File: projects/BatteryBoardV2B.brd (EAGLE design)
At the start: 90.6 x 96 mm, 225 parts, among them M1 BSO201SP, SW1 BTS50015-1TAD, SW2 BTS50015-1TAD, T1 AD590FLATPACK, T2 AD590FLATPACK, T3 AD590FLATPACK, T4 AD590FLATPACK, U1 TCA9535PWR, U10 LT1962-3, U11 LT1962-3, U12 LTC4411, U13 LTC4411, U14 LTC4121, U15 VNS3NV04DP-E, U16 LTC4121, U17 VNS3NV04DP-E, U18 AD8418, U19 AD8418, U2 AD7991-0, U3 LTC4412MPS6, U4 LTC4121-4.2, U5 LTC4121-4.2, U6 LC05111C13MTTTG, U7 LC05111C13MTTTG, U8 AD8418, U9 AD8418

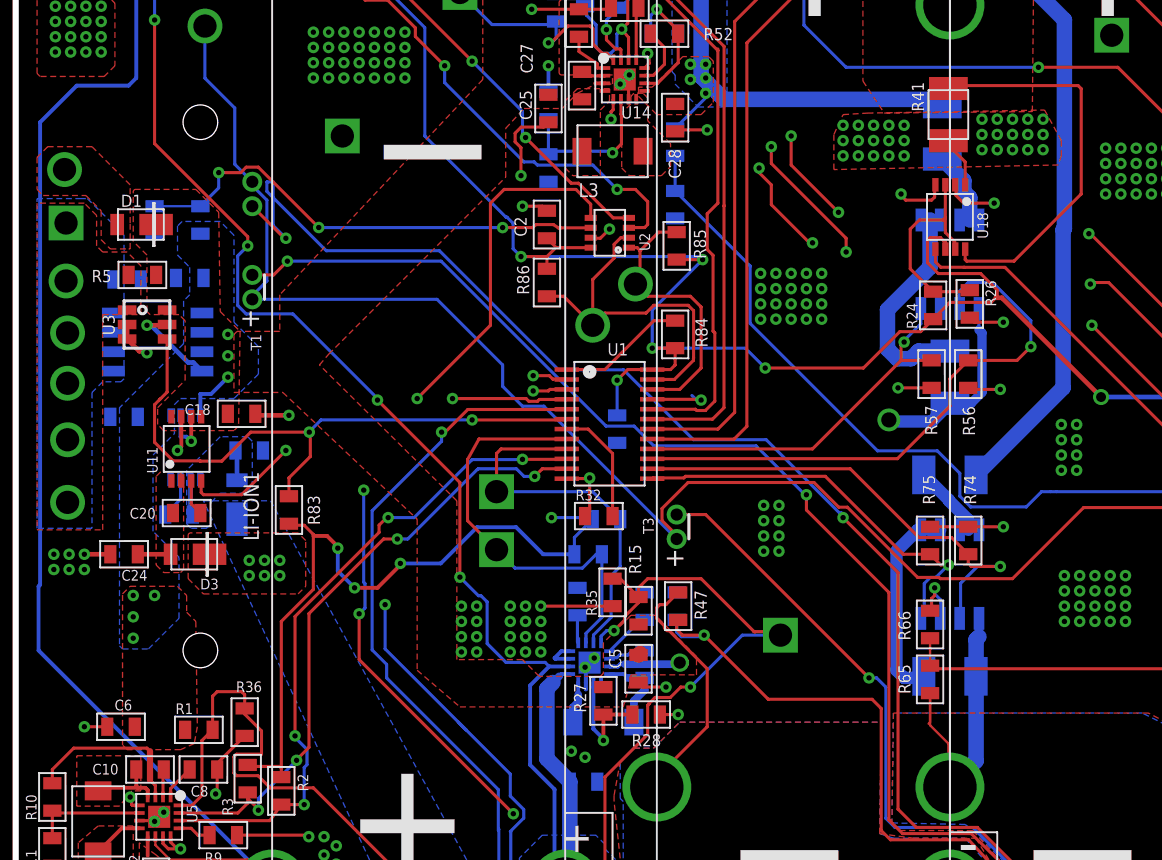
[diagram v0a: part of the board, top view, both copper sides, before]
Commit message: Updating schematic for battery board, adding schematic for flight configuration
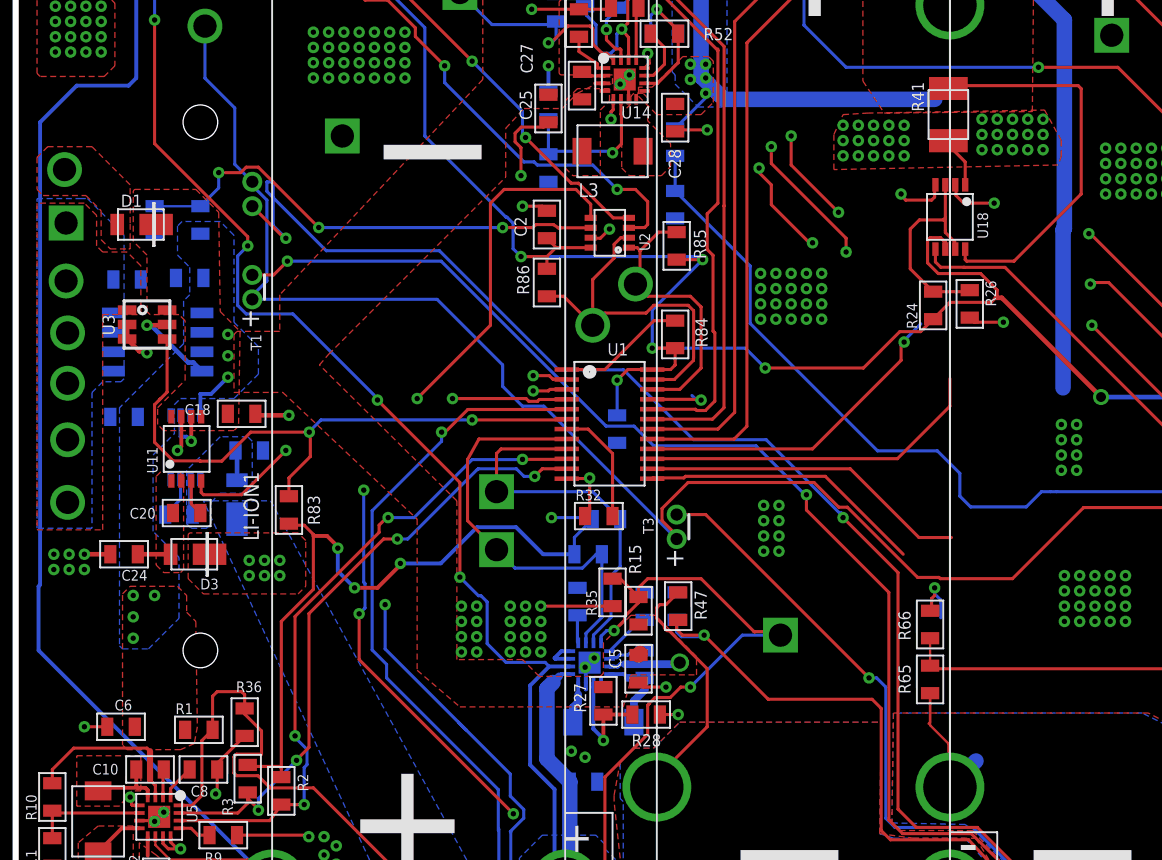
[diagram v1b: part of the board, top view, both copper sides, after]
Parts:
- removed R5: 0R, BrownSpaceEngineering:0805
- removed R54, R55, R72, R73: 34.8R@1W, BrownSpaceEngineering:1210
- removed R56, R57, R74, R75: 100K, BrownSpaceEngineering:0805
- removed U15, U17: VNS3NV04DP-E, BrownSpaceEngineering:SO-8
- R41, R59: value 0.001R@1W -> 0.001R@3W
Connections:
- removed net N$24: R54.P$1, U15.P$7, U15.P$8
- removed net N$25: R55.P$2, U15.P$5, U15.P$6
- removed net N$42: R72.P$1, U17.P$7, U17.P$8
- removed net N$43: R73.P$2, U17.P$5, U17.P$6
- net GND: no longer R56.1, R57.1, R74.1, R75.1, U15.P$3, U17.P$3
- net LF_B1_BT: no longer R57.2, U15.P$4
- net LF_B1_TT: no longer R56.2, U15.P$2
- net LF_B2_BT: no longer R75.2, U17.P$4
- net LF_B2_TT: no longer R74.2, U17.P$2
- net LIFE1: no longer R54.P$2
- net LIFE2: no longer R55.P$1, U15.P$1
- net LIFE3: no longer R72.P$2
- net LIFE4: no longer R73.P$1, U17.P$1
- net SP_C: no longer R5.1
- net SP_OUT: no longer R5.2
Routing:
- net LIFE2: track 54.9 -> 18.0 mm, vias 1 -> 0
- net N$25: track 15.5 -> 0.00 mm
- net LF_B1_TT: track 37.7 -> 22.7 mm, vias 1 -> 0
- net N$43: track 13.3 -> 0.00 mm
- net LF_B2_TT: track 31.2 -> 21.5 mm, vias 1 -> 0
- net LIFE4: track 20.6 -> 11.1 mm
- net GND: track 162.7 -> 153.5 mm, vias 310 -> 307
- net LIFE3: track 68.0 -> 59.9 mm
- net LF_B2_BT: track 26.3 -> 18.6 mm, vias 1 -> 0
- net N$42: track 6.08 -> 0.00 mm
- net N$24: track 6.01 -> 0.00 mm
- net LF_B1_BT: track 24.6 -> 21.6 mm
- net LIFE1: track 28.2 -> 27.5 mm

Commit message: wtf
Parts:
- R12, R31: value 0.13R@1W -> 0.025R@1W
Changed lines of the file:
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@@
 <attribute name="NAME" x="35.189" y="20.7145" size="0.8" layer="25" rot="R180"/>
 </element>
-<element name="R31" library="BrownSpaceEngineering" package="1210" value="0.13R@1W" x="2.8" y="88.1" smashed="yes" rot="MR270">
+<element name="R31" library="BrownSpaceEngineering" package="1210" value="0.025R@1W" x="2.8" y="88.1" smashed="yes" rot="MR270">
 <attribute name="NAME" x="2.27" y="86.246" size="0.8" layer="26" rot="MR180"/>
 </element>
@@
 <attribute name="NAME" x="8.8" y="27.14" size="1.4" layer="26" rot="MR270"/>
 </element>
-<element name="R12" library="BrownSpaceEngineering" package="1210" value="0.13R@1W" x="11.8" y="81.7"/>
+<element name="R12" library="BrownSpaceEngineering" package="1210" value="0.025R@1W" x="11.8" y="81.7"/>
 <element name="R16" library="BrownSpaceEngineering" package="0805" value="150K" x="5.3" y="10.1" smashed="yes" rot="R90">
 <attribute name="NAME" x="4.1691125" y="9.168340625" size="0.7" layer="25" rot="R90"/>
